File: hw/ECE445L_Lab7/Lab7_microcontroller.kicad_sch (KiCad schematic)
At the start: 21 parts, among them Y1 16MHz, Y2 16MHz

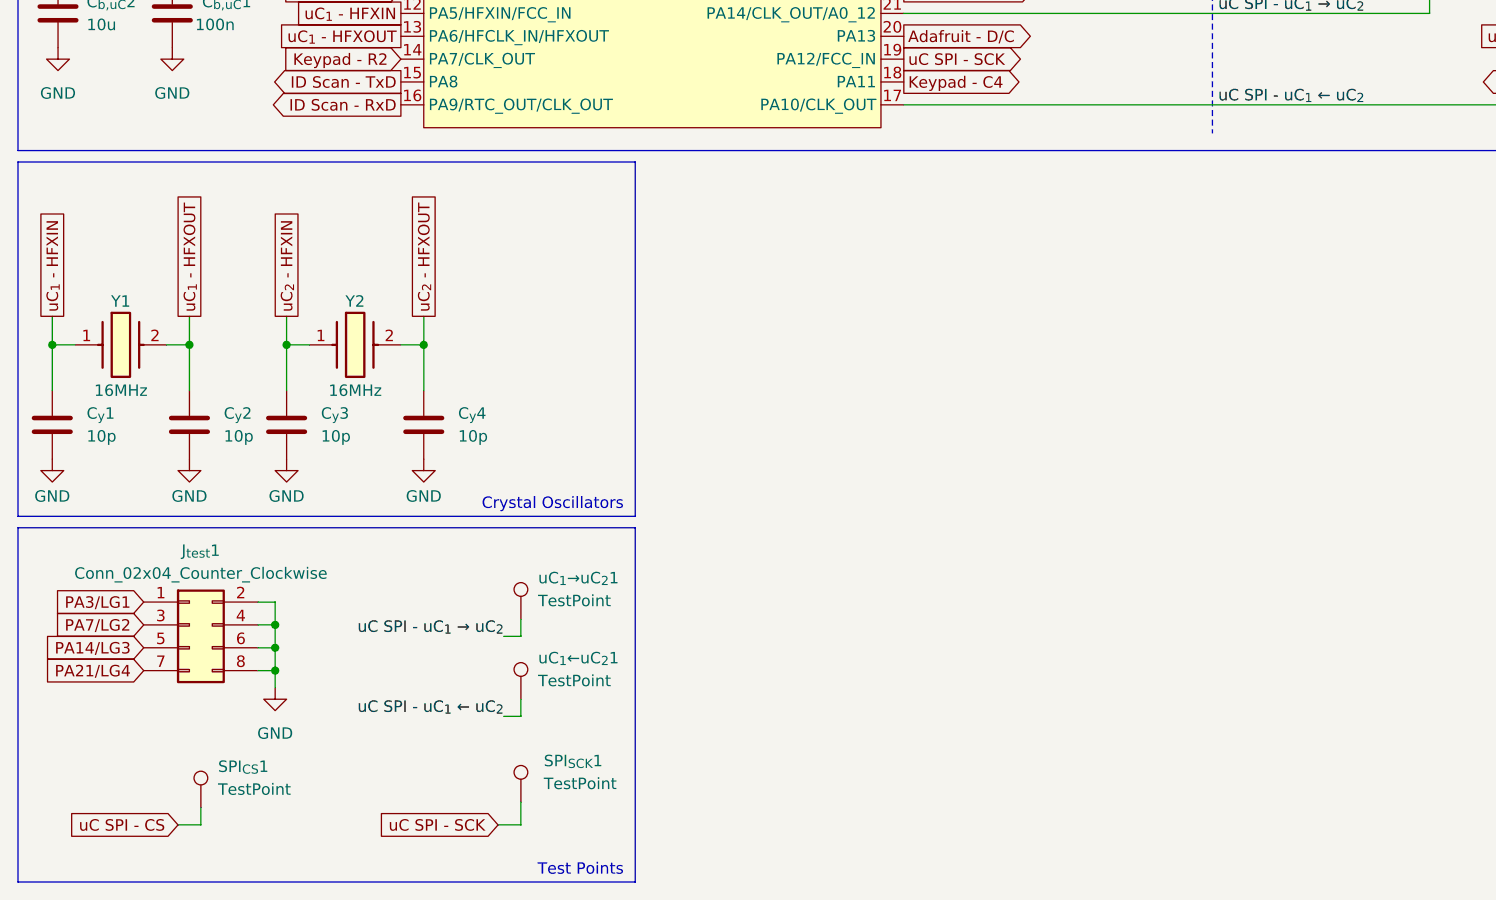
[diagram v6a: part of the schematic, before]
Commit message: started pcb layout
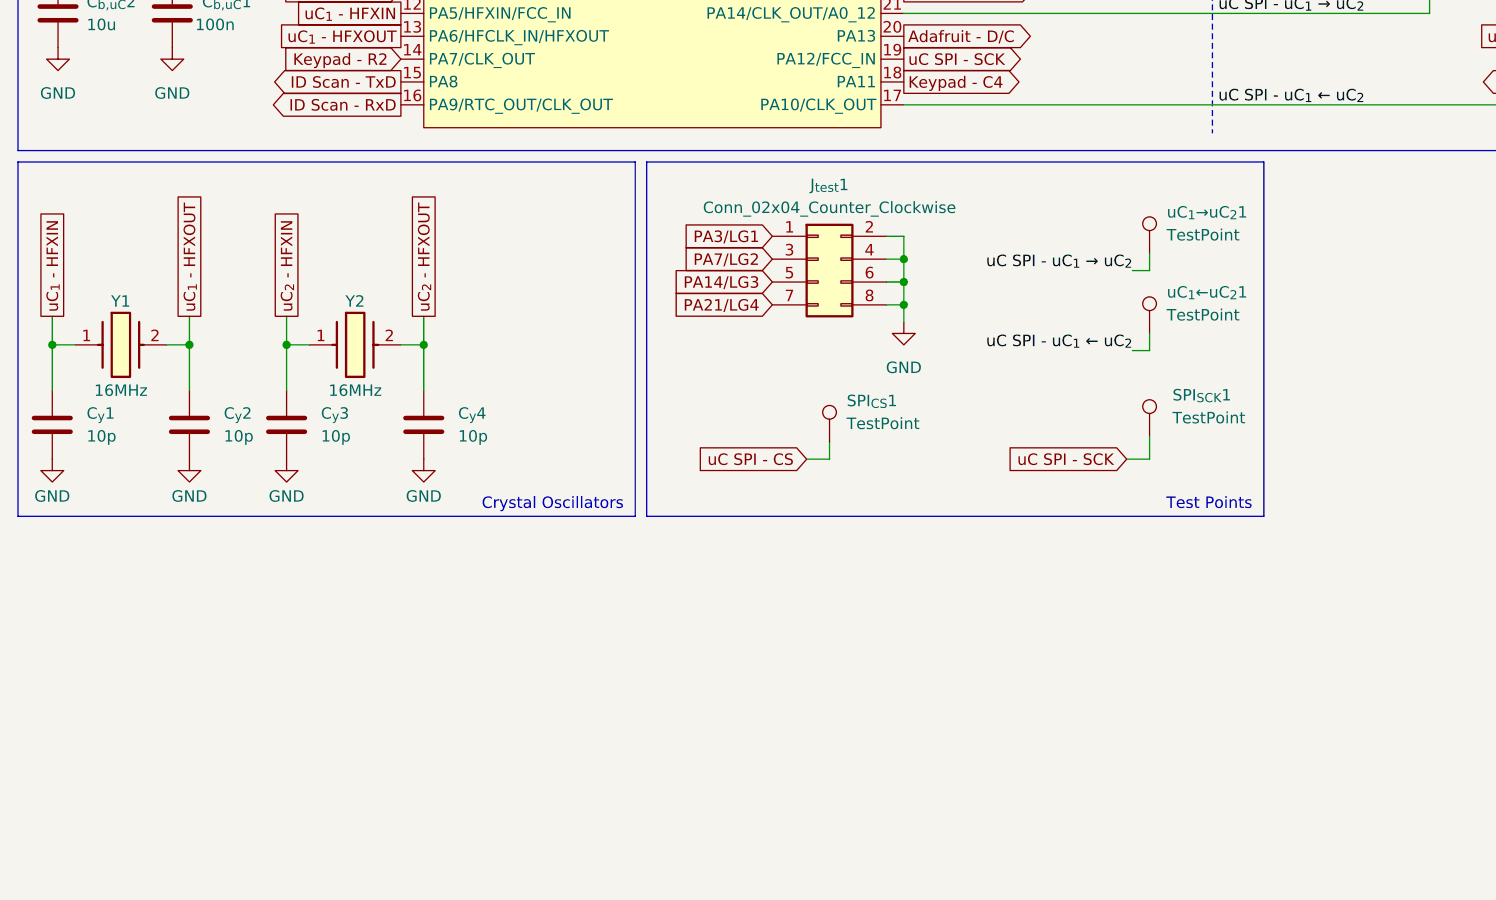
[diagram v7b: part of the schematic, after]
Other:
- moved on the sheet: J_{test}1, SPI_{CS}1, SPI_{SCK}1, uC_{1}←uC_{2}1, uC_{1}→uC_{2}1

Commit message: handoff to jonathan until midnight
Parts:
- C_{core}1, C_{core}2: Distributor Mouser -> Valvano
- Y1, Y2: Distributor (none) -> Valvano
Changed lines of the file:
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@@
 			)
 		)
+		(property "Distributor" "Valvano"
+			(at 20.32 135.89 0)
+			(hide yes)
+			(show_name no)
+			(do_not_autoplace no)
+			(effects
+				(font
+					(size 1.27 1.27)
+				)
+			)
+		)
 		(pin "2"
 		)
@@
 			)
 		)
-		(property "Distributor" "Mouser"
+		(property "Distributor" "Valvano"
 			(at 29.21 73.66 0)
 			(hide yes)
@@
 			)
 		)
-		(property "Distributor" "Mouser"
+		(property "Distributor" "Valvano"
 			(at 156.845 71.12 0)
 			(hide yes)
@@
 			(at 46.355 135.89 0)
 			(hide yes)
+			(show_name no)
+			(do_not_autoplace no)
+			(effects
+				(font
+					(size 1.27 1.27)
+				)
+			)
+		)
+		(property "Distributor" "Valvano"
+			(at 46.355 135.89 0)
+			(hide yes)
